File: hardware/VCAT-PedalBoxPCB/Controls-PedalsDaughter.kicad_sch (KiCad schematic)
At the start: 23 parts, among them J1 MX150_02x03_Vertical, J3 Conn_02x03_Top_Bottom, J4 Conn_02x06_Top_Bottom, J5 Conn_02x04_Top_Bottom, J6 MX150_02x10_Vertical

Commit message: IM DONNEEEE
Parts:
- R47: value 1.1k -> 10k
- Raw6: footprint TestPoint:TestPoint_THTPad_1.5x1.5mm_Drill0.7mm -> TestPoint:TestPoint_Keystone_5005-5009_Compact
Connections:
- net +3.3V: no longer names the net of PSOM1.2 (+3.3v)
- net +5V renamed +5V_Pots
- net 5V_BrakeFL renamed +5V_BrakeFL
- no-connect marks 32 -> 33
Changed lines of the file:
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@@
 	)
 	(no_connect
+		(at 245.11 43.942)
+	)
+	(no_connect
 		(at 159.004 -49.276)
 	)
@@
 	(wire
 		(pts
-			(xy 245.11 43.942) (xy 250.19 43.942)
-		)
-		(stroke
-			(width 0)
-			(type default)
-		)
-	)
-	(wire
-		(pts
 			(xy 139.192 90.424) (xy 142.494 90.424)
 		)
@@
 	(wire
 		(pts
-			(xy 56.134 139.954) (xy 58.166 139.954)
+			(xy 56.134 139.954) (xy 60.452 139.954)
 		)
 		(stroke
@@
 	(wire
 		(pts
-			(xy 250.19 43.942) (xy 252.222 41.91)
-		)
-		(stroke
-			(width 0)
-			(type default)
-		)
-	)
-	(wire
-		(pts
 			(xy 165.1 165.862) (xy 165.1 170.18)
 		)
@@
 	(wire
 		(pts
-			(xy 58.166 139.954) (xy 59.69 138.43)
-		)
-		(stroke
-			(width 0)
-			(type default)
-		)
-	)
-	(wire
-		(pts
 			(xy 129.286 72.898) (xy 128.016 74.168)
 		)
@@
 	(wire
 		(pts
+			(xy 60.452 139.954) (xy 61.722 138.684)
+		)
+		(stroke
+			(width 0)
+			(type default)
+		)
+	)
+	(wire
+		(pts
 			(xy 139.192 85.344) (xy 142.494 85.344)
 		)
@@
 		)
 	)
-	(label "5V_BrakeFL"
-		(at 59.69 138.43 0)
-		(effects
-			(font
-				(size 1.27 1.27)
-			)
-			(justify left bottom)
-		)
-	)
 	(label "BrakeFLRed_Amp"
 		(at 99.06 140.462 0)
@@
 		)
 	)
-	(label "5V_BrakeFL"
-		(at 116.84 63.246 180)
-		(effects
-			(font
-				(size 1.27 1.27)
-			)
-			(justify right bottom)
-		)
-	)
 	(label "AccelPotStatus"
 		(at 247.65 56.642 0)
@@
 	(symbol
 		(lib_id "power:+5V")
+		(at 116.84 63.246 0)
+		(unit 1)
+		(exclude_from_sim no)
+		(in_bom yes)
+		(on_board yes)
+		(dnp no)
+		(property "Reference" "#PWR040"
+			(at 116.84 67.056 0)
+			(effects
+				(font
+					(size 1.27 1.27)
+				)
+				(hide yes)
+			)
+		)
+		(property "Value" "+5V_BrakeFL"
+			(at 118.11 59.436 0)
+			(effects
+				(font
+					(size 1.27 1.27)
+				)
+			)
+		)
+		(property "Footprint" ""
+			(at 116.84 63.246 0)
+			(effects
+				(font
+					(size 1.27 1.27)
+				)
+				(hide yes)
+			)
+		)
+		(property "Datasheet" ""
+			(at 116.84 63.246 0)
+			(effects
+				(font
+					(size 1.27 1.27)
+				)
+				(hide yes)
+			)
+		)
+		(property "Description" "Power symbol creates a global label with name \"+5V\""
+			(at 116.84 63.246 0)
+			(effects
+				(font
+					(size 1.27 1.27)
+				)
+				(hide yes)
+			)
+		)
+		(pin "1"
+		)
+		(instances
+			(project "Controls-PedalsDaughter"
+				(path "/30d77876-714b-4f1b-9bad-b74eb43ddcf6"
+					(reference "#PWR040")
+					(unit 1)
+				)
+			)
+		)
+	)
+	(symbol
+		(lib_id "power:+5V")
 		(at 116.84 41.656 0)
 		(unit 1)
@@
 			)
 		)
-		(property "Value" "+5V"
-			(at 114.3 39.116 0)
+		(property "Value" "+5V_Pots"
+			(at 114.3 37.592 0)
 			(effects
 				(font
@@
 			)
 		)
-		(property "Footprint" "TestPoint:TestPoint_THTPad_1.5x1.5mm_Drill0.7mm"
+		(property "Footprint" "TestPoint:TestPoint_Keystone_5005-5009_Compact"
 			(at 196.596 129.794 0)
 			(effects
@@
 	)
 	(symbol
-		(lib_id "power:+3.3V")
-		(at 252.222 41.91 0)
+		(lib_id "power:VDDA")
+		(at 254.762 45.72 0)
 		(unit 1)
 		(exclude_from_sim no)
@@
 		(on_board yes)
 		(dnp no)
-		(fields_autoplaced yes)
-		(property "Reference" "#PWR013"
-			(at 252.222 45.72 0)
+		(property "Reference" "#PWR014"
+			(at 254.762 49.53 0)
 			(effects
 				(font
@@
 			)
 		)
-		(property "Value" "+3.3V"
-			(at 252.222 36.83 0)
+		(property "Value" "+VDDA"
+			(at 258.572 43.18 0)
 			(effects
 				(font
@@
 		)
 		(property "Footprint" ""
-			(at 252.222 41.91 0)
+			(at 254.762 45.72 0)
 			(effects
 				(font
@@
 		)
 		(property "Datasheet" ""
-			(at 252.222 41.91 0)
+			(at 254.762 45.72 0)
 			(effects
 				(font
@@
 			)
 		)
-		(property "Description" "Power symbol creates a global label with name \"+3.3V\""
-			(at 252.222 41.91 0)
+		(property "Description" "Power symbol creates a global label with name \"VDDA\""
+			(at 254.762 45.72 0)
 			(effects
 				(font
@@
 			(project ""
 				(path "/30d77876-714b-4f1b-9bad-b74eb43ddcf6"
-					(reference "#PWR013")
+					(reference "#PWR014")
 					(unit 1)
 				)
@@
 	)
 	(symbol
-		(lib_id "power:VDDA")
-		(at 254.762 45.72 0)
+		(lib_id "power:+5V")
+		(at 61.722 138.684 0)
 		(unit 1)
 		(exclude_from_sim no)
@@
 		(on_board yes)
 		(dnp no)
-		(property "Reference" "#PWR014"
-			(at 254.762 49.53 0)
+		(property "Reference" "#PWR039"
+			(at 61.722 142.494 0)
 			(effects
 				(font
@@
 			)
 		)
-		(property "Value" "+VDDA"
-			(at 258.572 43.18 0)
+		(property "Value" "+5V_BrakeFL"
+			(at 62.992 134.874 0)
 			(effects
 				(font
@@
 		)
 		(property "Footprint" ""
-			(at 254.762 45.72 0)
+			(at 61.722 138.684 0)
 			(effects
 				(font
@@
 		)
 		(property "Datasheet" ""
-			(at 254.762 45.72 0)
+			(at 61.722 138.684 0)
 			(effects
 				(font
@@
 			)
 		)
-		(property "Description" "Power symbol creates a global label with name \"VDDA\""
-			(at 254.762 45.72 0)
+		(property "Description" "Power symbol creates a global label with name \"+5V\""
+			(at 61.722 138.684 0)
 			(effects
 				(font
@@
 		)
 		(instances
-			(project ""
+			(project "Controls-PedalsDaughter"
 				(path "/30d77876-714b-4f1b-9bad-b74eb43ddcf6"
-					(reference "#PWR014")
+					(reference "#PWR039")
 					(unit 1)
 				)
@@
 			)
 		)
-		(property "Value" "1.1k"
-			(at 159.258 138.43 90)
+		(property "Value" "10k"
+			(at 158.75 138.176 90)
 			(effects
 				(font
@@
 	)
 	(symbol
+		(lib_id "power:+5V")
+		(at 61.976 127.762 0)
+		(unit 1)
+		(exclude_from_sim no)
+		(in_bom yes)
+		(on_board yes)
+		(dnp no)
+		(property "Reference" "#PWR045"
+			(at 61.976 131.572 0)
+			(effects
+				(font
+					(size 1.27 1.27)
+				)
+				(hide yes)
+			)
+		)
+		(property "Value" "+5V_Pots"
+			(at 61.722 123.698 0)
+			(effects
+				(font
+					(size 1.27 1.27)
+				)
+			)
+		)
+		(property "Footprint" ""
+			(at 61.976 127.762 0)
+			(effects
+				(font
+					(size 1.27 1.27)
+				)
+				(hide yes)
+			)
+		)
+		(property "Datasheet" ""
+			(at 61.976 127.762 0)
+			(effects
+				(font
+					(size 1.27 1.27)
+				)
+				(hide yes)
+			)
+		)
+		(property "Description" "Power symbol creates a global label with name \"+5V\""
+			(at 61.976 127.762 0)
+			(effects
+				(font
+					(size 1.27 1.27)
+				)
+				(hide yes)
+			)
+		)
+		(pin "1"
+		)
+		(instances
+			(project "Controls-PedalsDaughter"
+				(path "/30d77876-714b-4f1b-9bad-b74eb43ddcf6"
+					(reference "#PWR045")
+					(unit 1)
+				)
+			)
+		)
+	)
+	(symbol
 		(lib_id "Mechanical:MountingHole")
 		(at 227.33 127 0)
@@
 					(unit 1)
 				)
-			)
-		)
-	)
-	(symbol
-		(lib_id "power:+5V")
-		(at 61.976 127.762 0)
-		(unit 1)
-		(exclude_from_sim no)
-		(in_bom yes)
-		(on_board yes)
-		(dnp no)
-		(fields_autoplaced yes)
-		(property "Reference" "#PWR02"
-			(at 61.976 131.572 0)
-			(effects
-				(font
-					(size 1.27 1.27)
-				)
-				(hide yes)
-			)
-		)
-		(property "Value" "+5V"
-			(at 61.976 123.317 0)
-			(effects
-				(font
-					(size 1.27 1.27)
-				)
-			)
-		)
-		(property "Footprint" ""
-			(at 61.976 127.762 0)
-			(effects
-				(font
-					(size 1.27 1.27)
-				)
-				(hide yes)
-			)
-		)
-		(property "Datasheet" ""
-			(at 61.976 127.762 0)
-			(effects
-				(font
-					(size 1.27 1.27)
-				)
-				(hide yes)
-			)
-		)
-		(property "Description" "Power symbol creates a global label with name \"+5V\""
-			(at 61.976 127.762 0)
-			(effects
-				(font
-					(size 1.27 1.27)
-				)
-				(hide yes)
-			)
-		)
-		(pin "1"
-		)
-		(instances
-			(project ""
-				(path "/30d77876-714b-4f1b-9bad-b74eb43ddcf6"
-					(reference "#PWR02")
-					(unit 1)
-				)

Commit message: Gerber + JLCpcb BOM :)
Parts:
- removed PWR_+24: PedalsBoard_Status_Red, LED_SMD:LED_0603_1608Metric_Pad1.05x0.95mm_HandSolder, symbol Device:LED
- added PWR24: 0603_SMD, LED_SMD:LED_0603_1608Metric_Pad1.05x0.95mm_HandSolder, symbol Device:LED
- J4: now left out of the parts list
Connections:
- net +24V: now also PWR24.2 (A)
- net at R47.1: now also PWR24.1 (K)

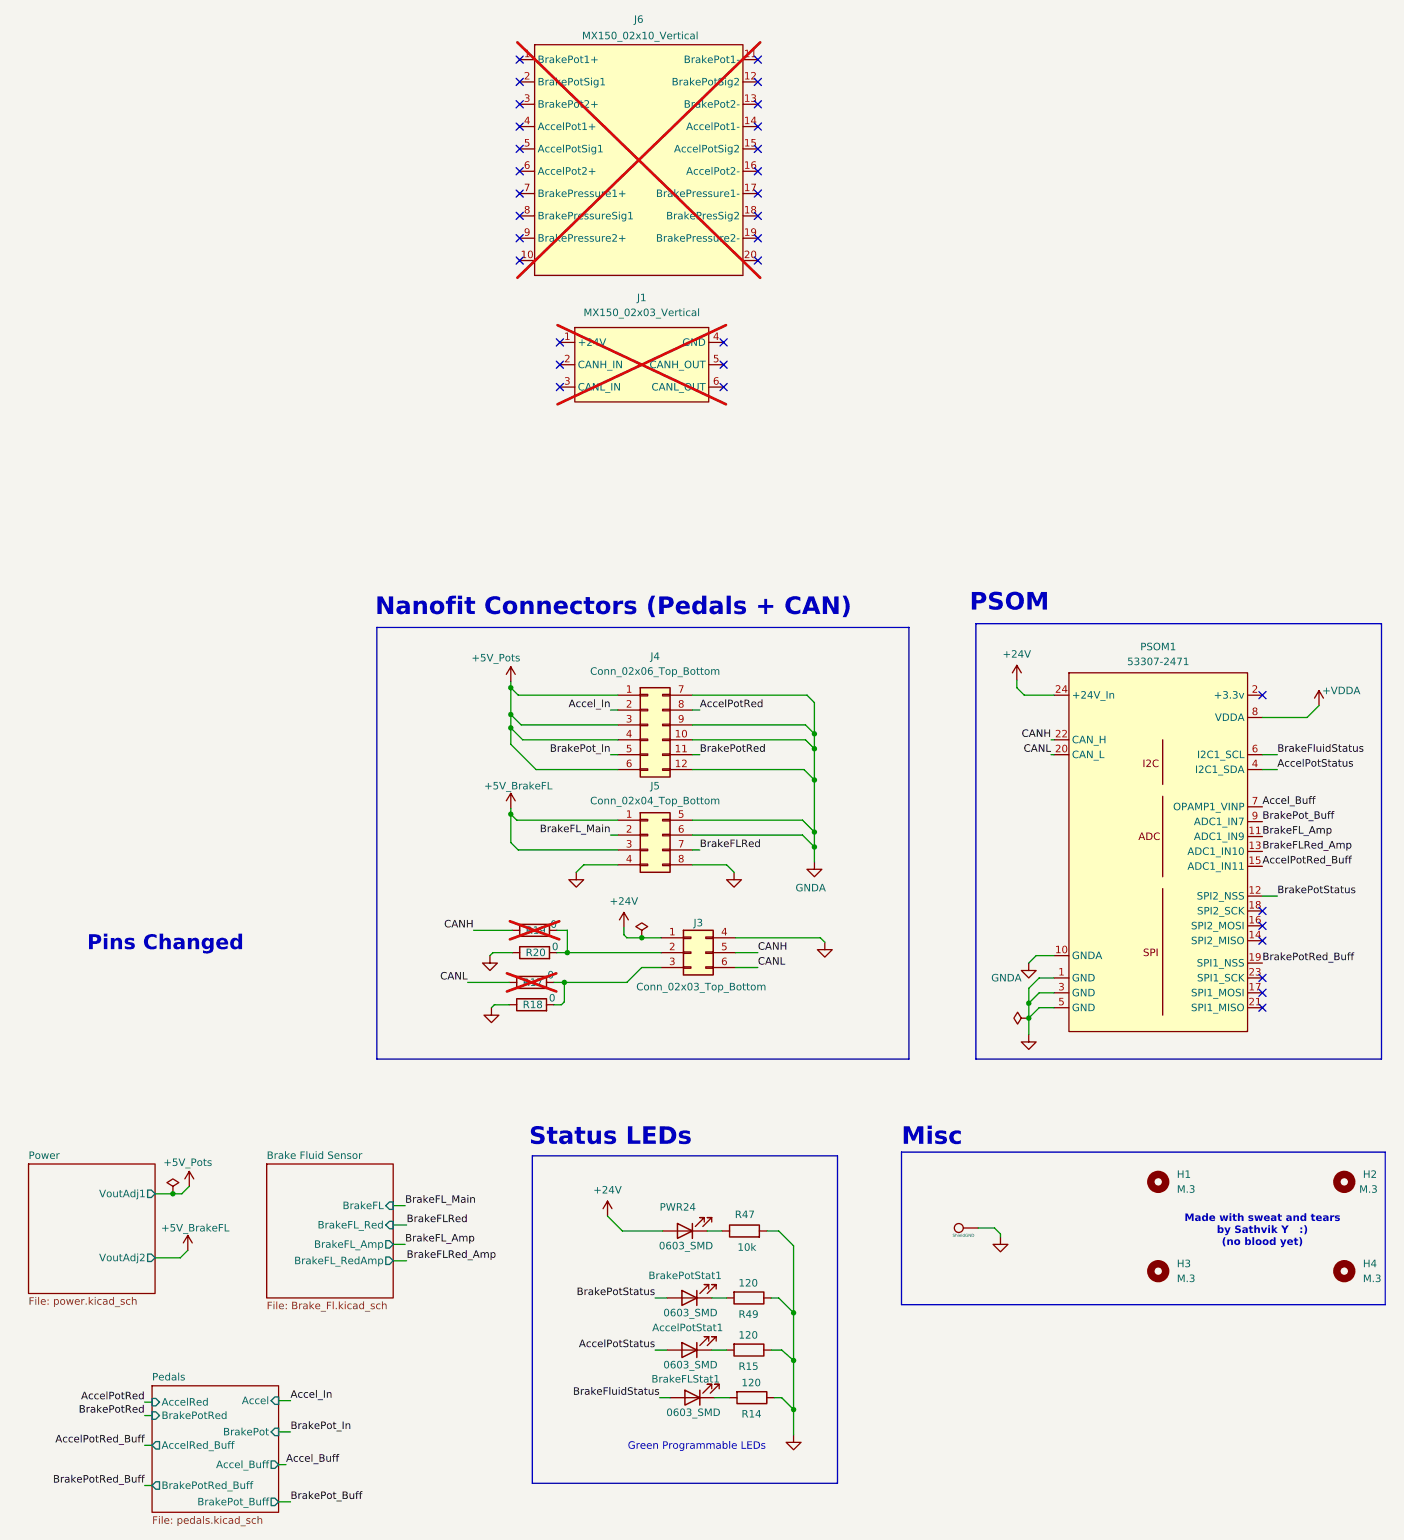
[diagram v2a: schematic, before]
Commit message: change VDDA to 3v3 on sch
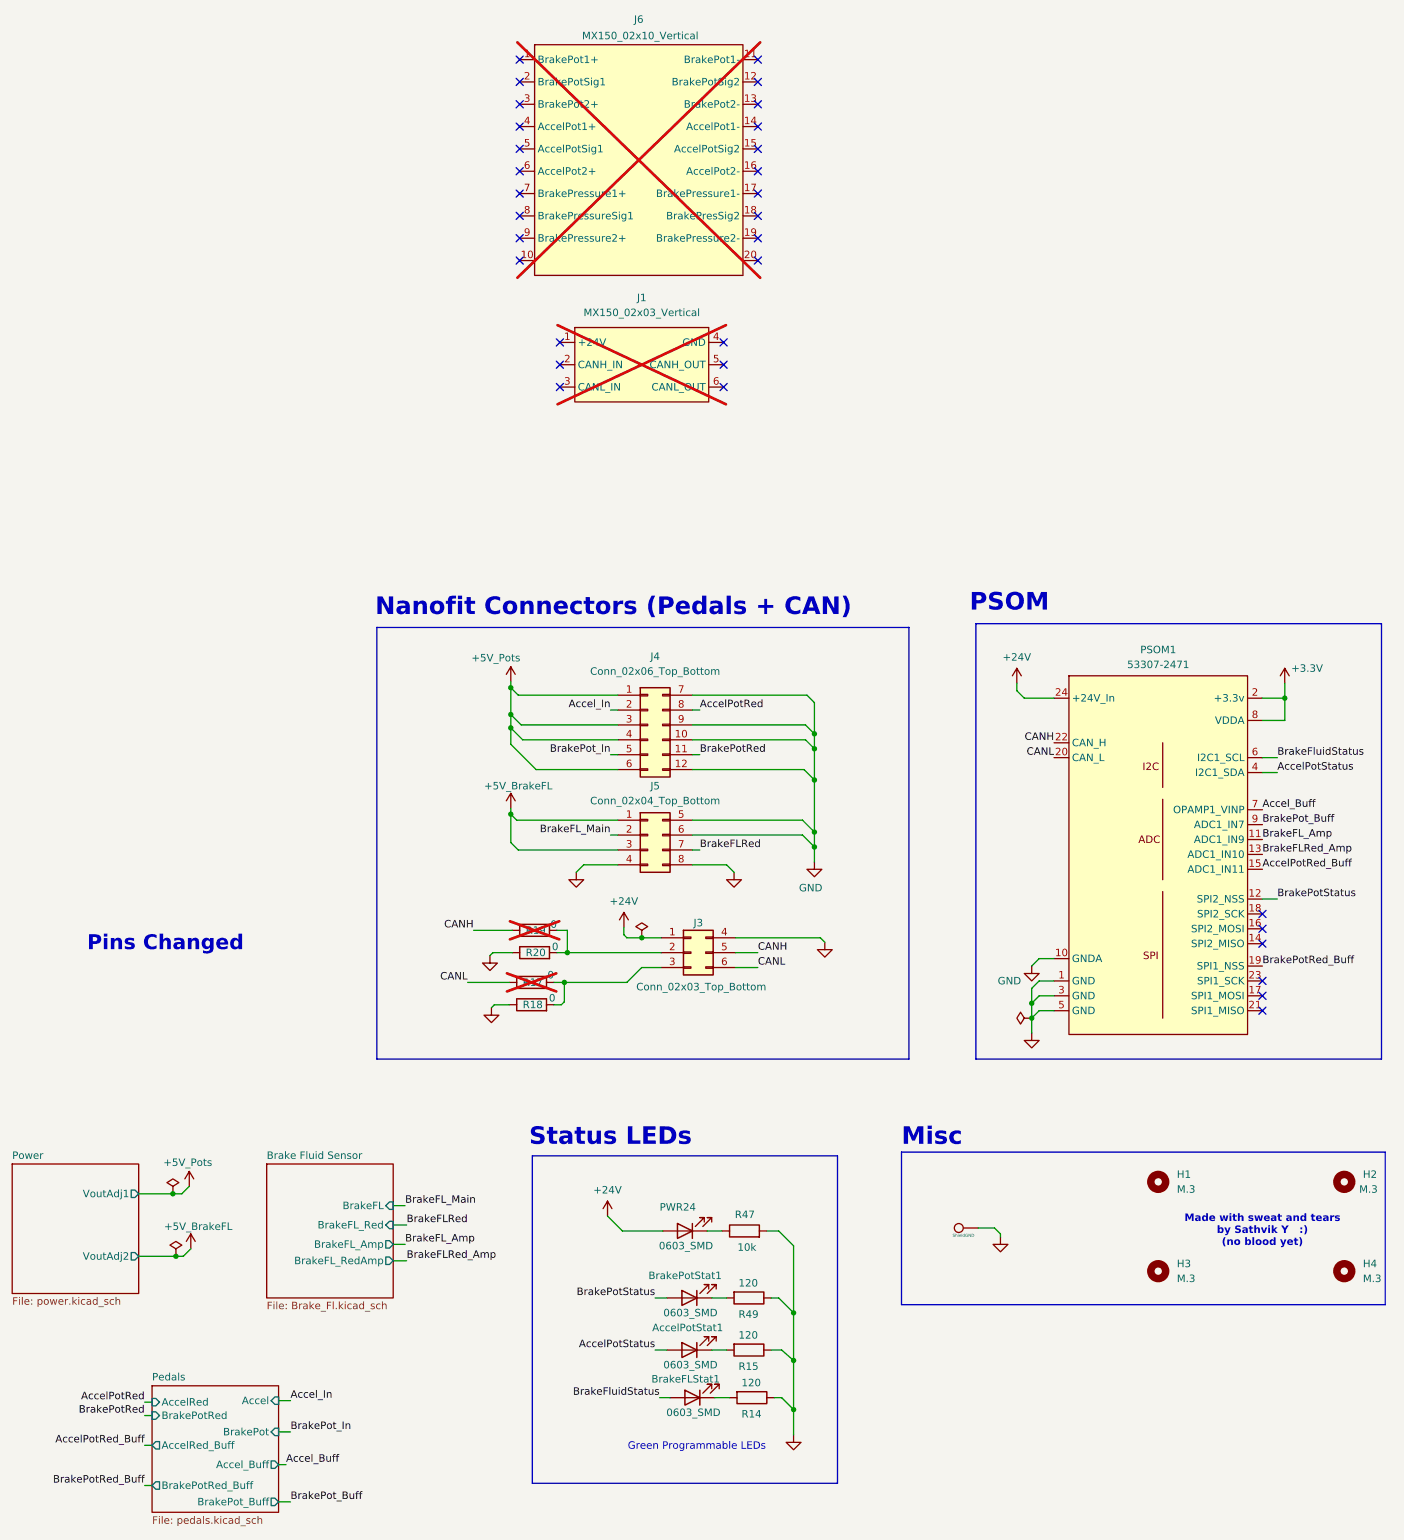
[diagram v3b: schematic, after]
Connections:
- net +VDDA is gone; now on net +3.3V: PSOM1.8 (VDDA)
- net GNDA is gone; now on net GND: J4.10 (Pin_10), J4.12 (Pin_12), J4.7 (Pin_7), J4.9 (Pin_9), J5.5 (Pin_5), J5.6 (Pin_6), PSOM1.10 (GNDA)
- net +3.3V: now reaches PSOM1.2 (+3.3v)
- no-connect marks 33 -> 32
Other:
- moved on the sheet: PSOM1
